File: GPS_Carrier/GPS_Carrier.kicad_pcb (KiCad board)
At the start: 4 copper layers, 90 x 55 mm, 21 parts, among them J1 Conn_01x01_Pin, J10 Conn_01x01_Pin, J11 Conn_01x01_Pin, J2 Conn_01x01_Pin, J3 Conn_01x01_Pin, J4 Conn_01x01_Pin, J5 Conn_01x01_Pin, J6 Conn_01x01_Pin, J7 Conn_01x01_Pin, J8 Conn_01x01_Pin, J9 Conn_01x01_Pin, U1 ATGM336H-5N31, U2 AT2659, U3 AMS1117-3.3_C347222, U4 BWU.FL-IPEX1

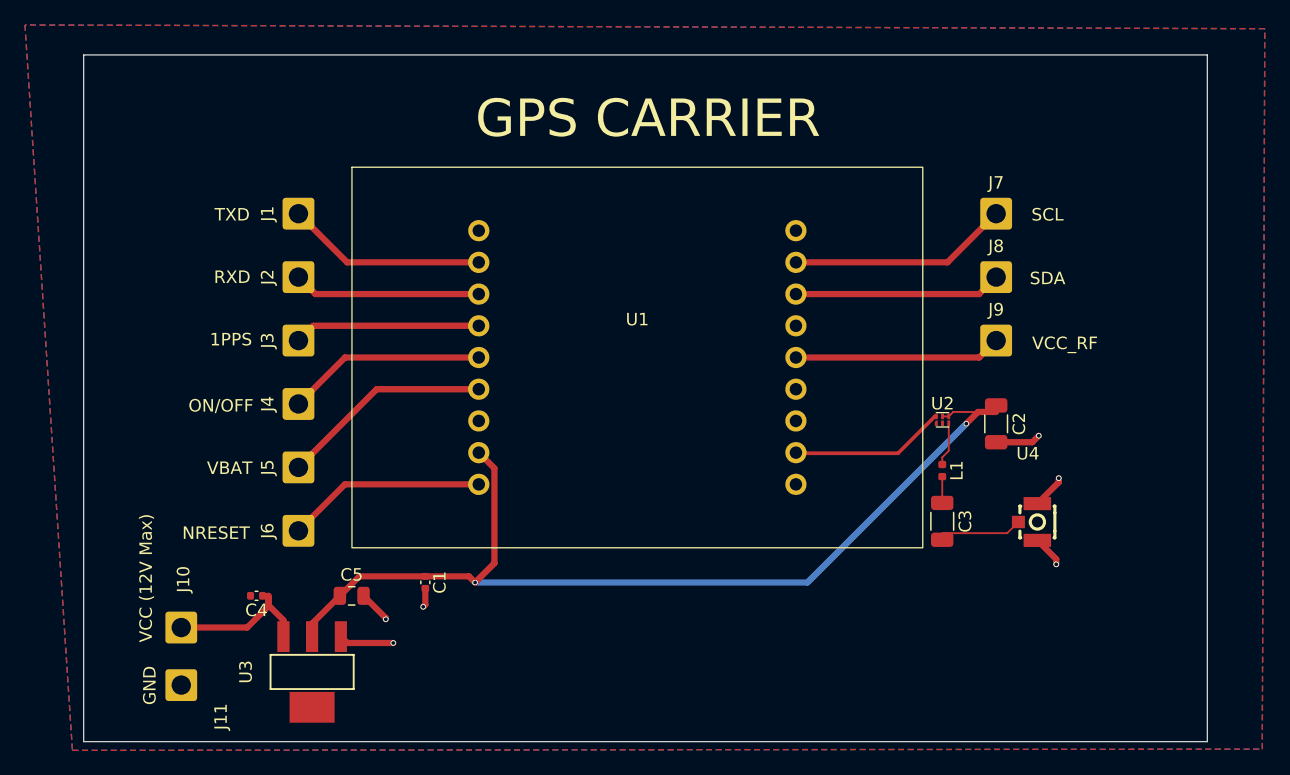
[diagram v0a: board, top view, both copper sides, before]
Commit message: RTC and GPS Breakouts Finished
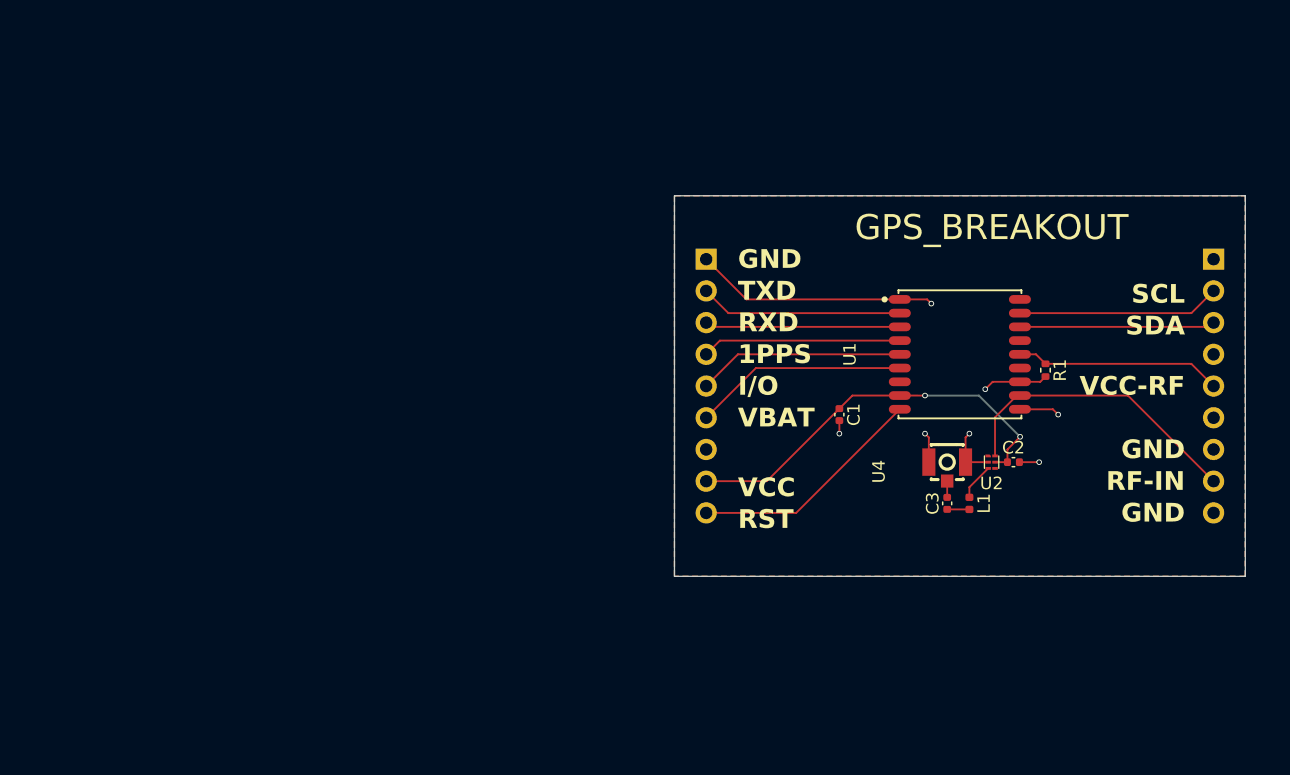
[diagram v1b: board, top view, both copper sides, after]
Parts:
- removed C4: 10uF, Capacitor_SMD:C_0402_1005Metric
- removed C5: 22uF, Capacitor_SMD:C_0805_2012Metric
- removed J10, J11, J3, J4, J5, J6, J7, J8, J9: Conn_01x01_Pin, Connector_Wire:SolderWire-0.75sqmm_1x01_D1.25mm_OD2.3mm
- removed U3: AMS1117-3.3_C347222, PARTS:SOT-223-4_L6.5-W3.5-P2.30-LS7.0-BR
- added R1: 1k, Resistor_SMD:R_0402_1005Metric, F.Cu at (177.0, 95.2)
- C2, C3: footprint Capacitor_SMD:C_1206_3216Metric -> Capacitor_SMD:C_0402_1005Metric
- J1, J2: value Conn_01x01_Pin -> Conn_01x09_Pin; footprint Connector_Wire:SolderWire-0.75sqmm_1x01_D1.25mm_OD2.3mm -> Connector_PinHeader_2.54mm:PinHeader_1x09_P2.54mm_Vertical; moved to B.Cu
- U1: footprint PARTS:RA_08H-BREAKOUT -> PARTS:GPSM-SMD_ATGM336H-TR
- moved J2 73.3 mm to (190.5, 86.4), turned to 180 degrees
- moved C1 35.8 mm to (160.5, 98.8)
- moved J1 32.9 mm to (149.9, 86.4), turned to 180 degrees
- moved U1 25.9 mm to (170.2, 94.0), turned to 90 degrees
- moved U4 7.62 mm to (169.2, 103.4), turned to 90 degrees
- moved U2 5.19 mm to (172.7, 102.6), turned to 0 degrees
- moved L1 3.41 mm to (170.9, 105.9)
- moved C2 3.37 mm to (174.5, 102.6), turned to 0 degrees
- moved C3 1.49 mm to (169.2, 105.9), turned to 90 degrees
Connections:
- C1 pad 1: +3.3V -> VCC
- C2 pad 1: +3.3V -> VCC
- J1 pad 1: Net-(J1-Pin_1) -> GND
- J2 pad 1: Net-(J2-Pin_1) -> unconnected-(J2-Pin_1-Pad1)
- U1 pad 11: Net-(U1-RF_IN) -> /RF_IN
- U1 pad 14: Net-(J9-Pin_1) -> /VCC_RF
- U1 pad 16: Net-(J8-Pin_1) -> /SDA
- U1 pad 17: Net-(J7-Pin_1) -> /SCL
- U1 pad 2: Net-(J1-Pin_1) -> /TXD
- U1 pad 3: Net-(J2-Pin_1) -> /RXD
- U1 pad 4: Net-(J3-Pin_1) -> /1PPS
- U1 pad 5: Net-(J4-Pin_1) -> /ON/OFF
- U1 pad 6: Net-(J5-Pin_1) -> /VBAT
- U1 pad 8: +3.3V -> VCC
- U1 pad 9: Net-(J6-Pin_1) -> /RST
- U2 pad 4: +3.3V -> VCC
- U2 pad 5: +3.3V -> VCC
- U2 pad 6: Net-(U1-RF_IN) -> /RF_IN
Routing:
- net +3.3V: track 78.0 -> 0.00 mm, vias 2 -> 0
- net /RF_IN: track 0.00 -> 24.2 mm
- net VCC: track 12.3 -> 32.8 mm, vias 0 -> 2
- net GND: track 17.5 -> 37.2 mm, vias 6 -> 7
- net /RST: track 0.00 -> 18.9 mm
- net Net-(J7-Pin_1): track 17.7 -> 0.00 mm
- net /VBAT: track 0.00 -> 17.2 mm
- net Net-(J5-Pin_1): track 17.0 -> 0.00 mm
- net Net-(J9-Pin_1): track 16.6 -> 0.00 mm
- net Net-(J8-Pin_1): track 16.6 -> 0.00 mm
- net /ON/OFF: track 0.00 -> 16.6 mm
- net /VCC_RF: track 0.00 -> 16.6 mm
- net /TXD: track 0.00 -> 16.2 mm
- net /SCL: track 0.00 -> 16.2 mm
- net Net-(J1-Pin_1): track 16.1 -> 0.00 mm
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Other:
- board size 90 x 55 mm -> 45.7 x 30.5 mm
- board text added: "GPS_BREAKOUT"
- board text added: "I/O"
- board text added: "RF-IN"
- board text added: "RST"
- board text added: "VCC"
- board text added: "VCC-RF"
- board text removed: "GPS CARRIER"
- board text removed: "NRESET"
- board text removed: "ON/OFF"
- board text removed: "VCC (12V Max)"
- board text removed: "VCC_RF"
